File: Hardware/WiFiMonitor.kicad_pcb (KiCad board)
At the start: 2 copper layers, 47.2 x 47.2 mm, 37 parts, among them J1 ADAP_ESP, J3 BATT, J5 FTDI, U1 4N25, U2 4N25, U3 4N25, U4 4N25, U5 MCP73831T-4ADI/OT, U6 AP1117-33, U7 DS3231MZ+

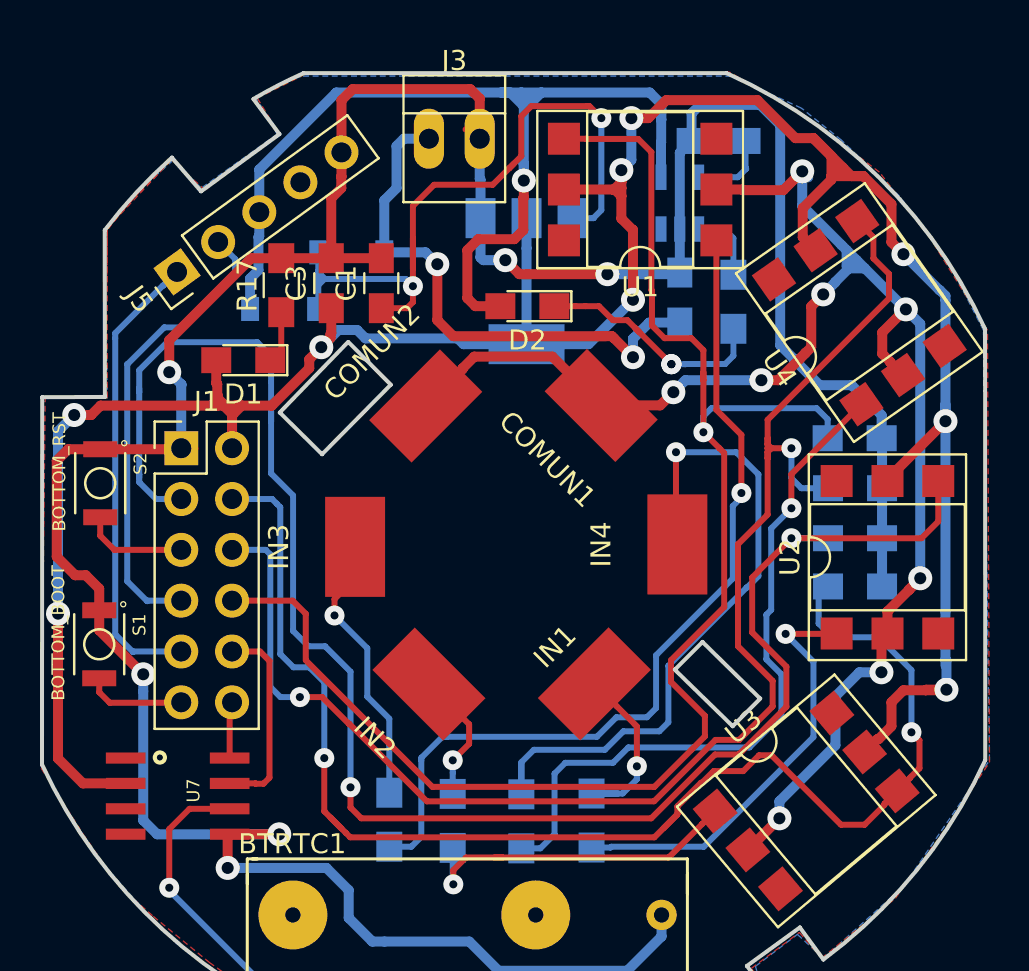
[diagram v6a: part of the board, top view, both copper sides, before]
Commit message: Fix vias at the power side, and fix labels
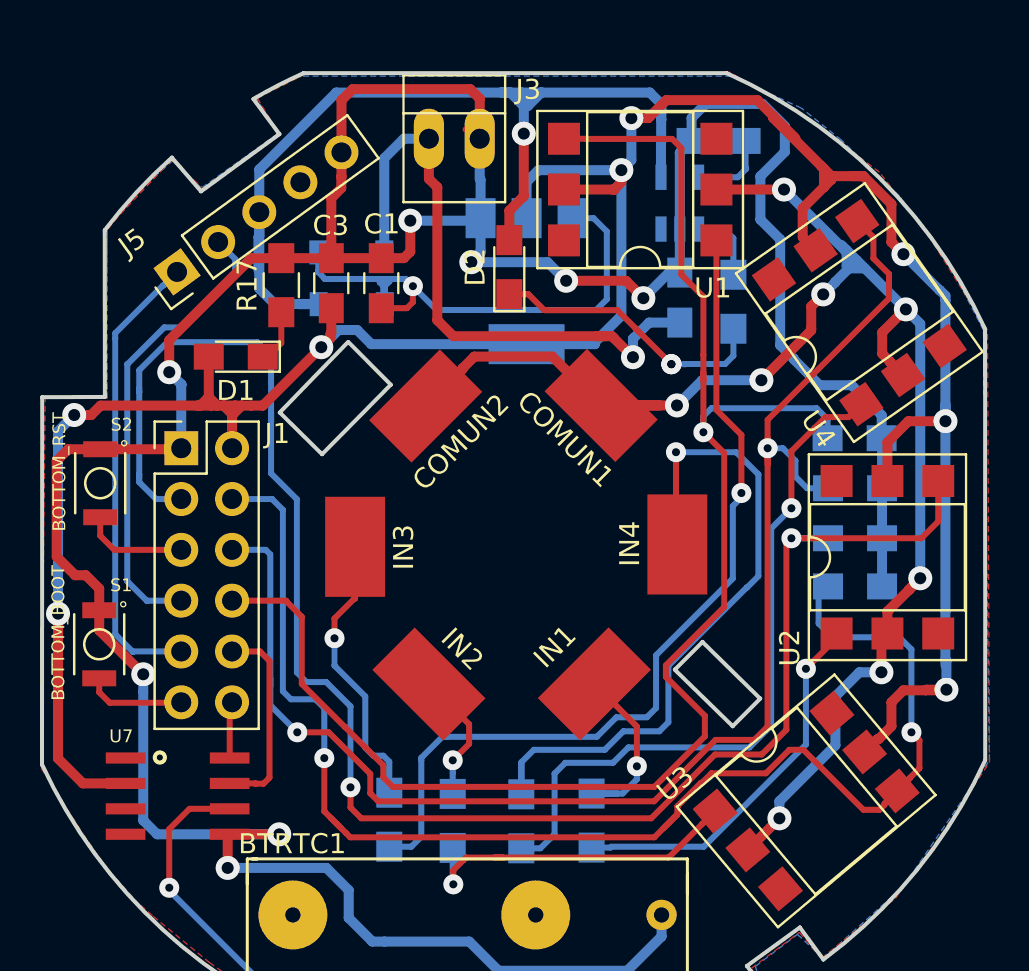
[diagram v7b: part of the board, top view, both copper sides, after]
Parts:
- moved D4 3.44 mm to (186.5, 79.8)
- moved D2 2.15 mm to (194.4, 78.0), turned to 90 degrees
- moved D1 0.41 mm to (180.7, 82.4)
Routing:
- net GND: track 155.7 -> 165.2 mm, vias 6 -> 8
- net Net-(C1-Pad1): track 36.5 -> 28.5 mm, vias 2 -> 1
- net /BAT: track 27.6 -> 31.2 mm, vias 2 -> 1
- net Net-(R4-Pad1): track 21.7 -> 19.1 mm
- net Net-(D2-Pad1): track 12.0 -> 14.5 mm
- net Net-(IN3-Pad1): track 15.6 -> 17.5 mm
- net /D2: track 76.6 -> 78.0 mm
- net /D3: track 72.9 -> 74.0 mm
- net +3V3: track 144.2 -> 143.4 mm, vias 9 -> 8
- net /D0: track 86.9 -> 86.2 mm
